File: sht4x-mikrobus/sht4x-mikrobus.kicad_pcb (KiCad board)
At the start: 2 copper layers, 25.4 x 29.2 mm, 8 parts, among them J1 MikroBus Left, J2 MikroBus Right, U1 SHT4x

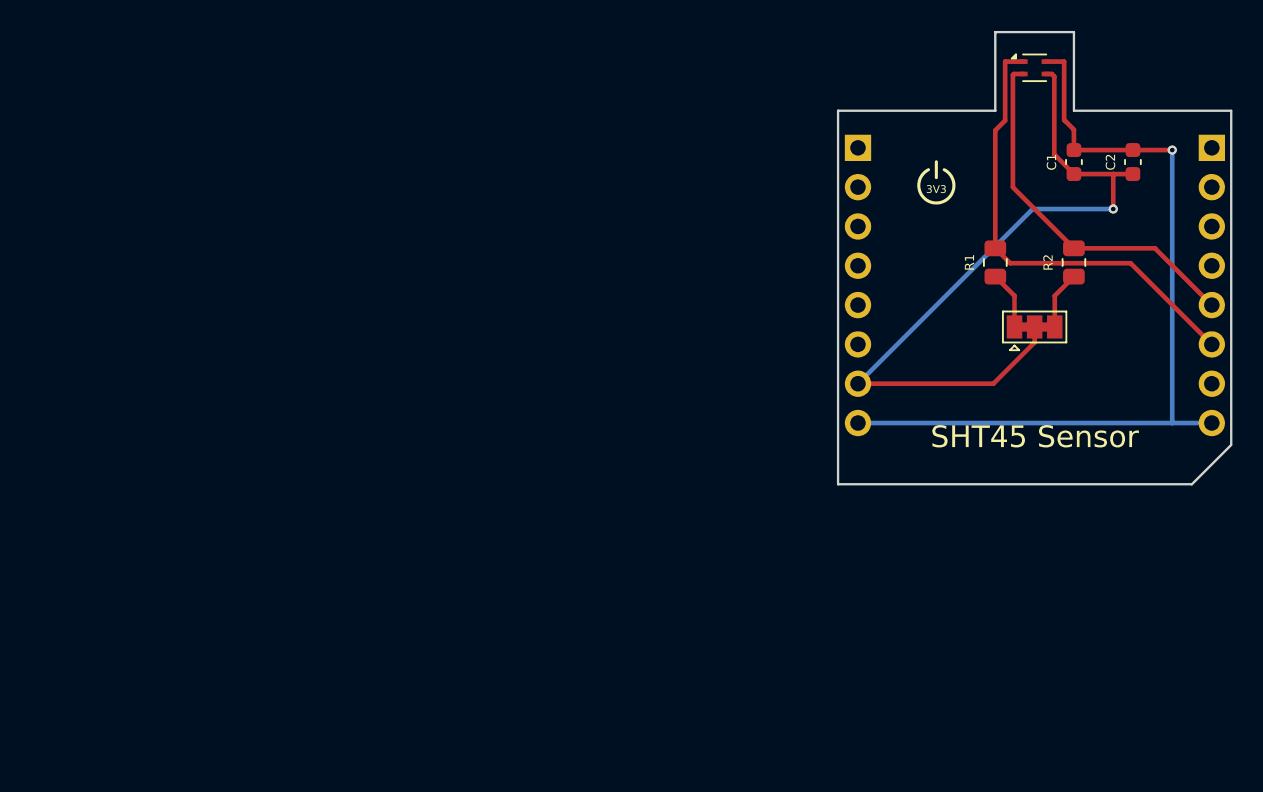
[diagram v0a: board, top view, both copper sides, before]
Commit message: Decided to completely redo the PCB added cuts on either sides of the sensor
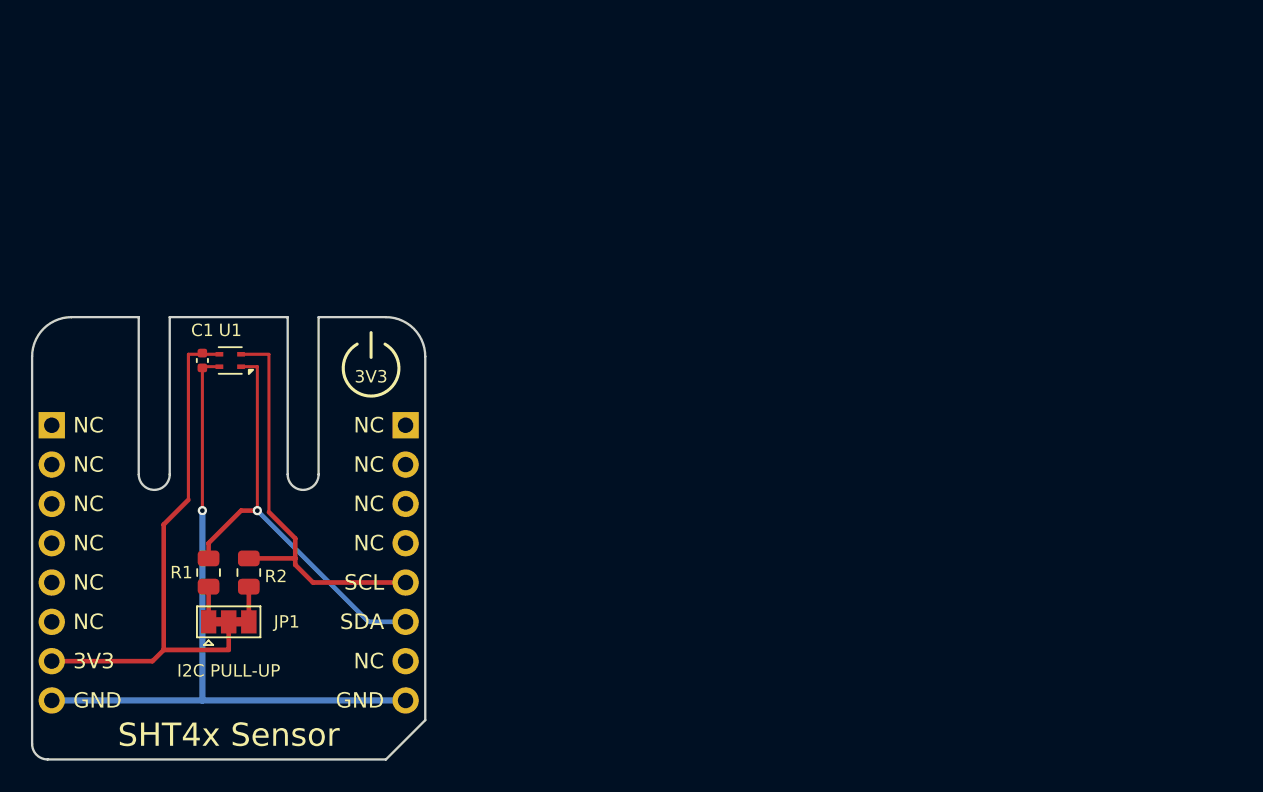
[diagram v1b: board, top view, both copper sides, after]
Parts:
- removed C2: 4.7uF, Capacitor_SMD:C_0603_1608Metric
- C1: footprint Capacitor_SMD:C_0603_1608Metric -> Capacitor_SMD:C_0402_1005Metric
- J1: value MikroBus Left -> Mikrobus Left
- J2: value MikroBus Right -> Mikrobus Right
- moved C1 57.8 mm to (146.9, 93.6), turned to -90 degrees
- moved R2 56.9 mm to (149.9, 107.3)
- moved JP1 55.4 mm to (148.6, 110.5)
- moved U1 55.3 mm to (148.7, 93.6), turned to 180 degrees
- moved J2 55.1 mm to (160.0, 97.8)
- moved J1 55.1 mm to (137.2, 97.8)
- moved R1 54.6 mm to (147.3, 107.3)
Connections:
- R1 pad 1: Net-(JP1-B) -> Net-(JP1-A)
- R2 pad 1: Net-(JP1-A) -> Net-(JP1-B)
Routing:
- net +3.3V: track 48.2 -> 35.3 mm, vias 1 -> 0
- net GND: track 54.0 -> 45.5 mm
- net SCL: track 24.0 -> 26.7 mm
- net SDA: track 30.1 -> 27.9 mm, vias 0 -> 1
- net Net-(JP1-A): track 3.77 -> 2.27 mm
- net Net-(JP1-B): track 3.77 -> 2.27 mm
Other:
- board size 25.4 x 29.2 mm -> 25.4 x 28.6 mm
- board text added: "GND"
- board text added: "I2C PULL-UP"
- board text added: "NC"
- board text added: "REV 2"
- board text added: "SCL"
- board text added: "SDA"
- board text added: "SHT4x Sensor"
- board text added: "aelius labs"
- board text removed: "SHT45 Sensor"
